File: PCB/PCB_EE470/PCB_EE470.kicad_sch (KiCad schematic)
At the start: 21 parts, among them IC1 LME49860MAX_NOPB, J1 Power, J2 Digital/PWM, J3 Analog, J4 Digital/PWM

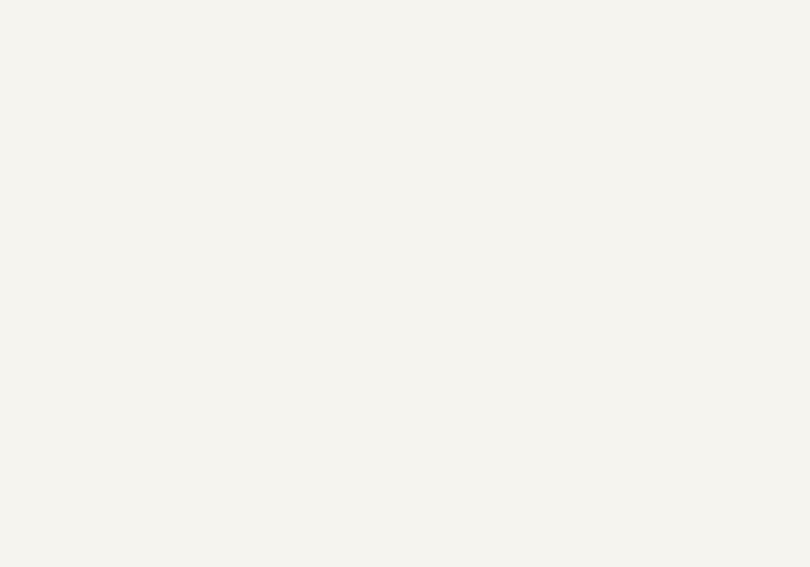
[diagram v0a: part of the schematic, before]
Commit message: ajout port jst écran arduino
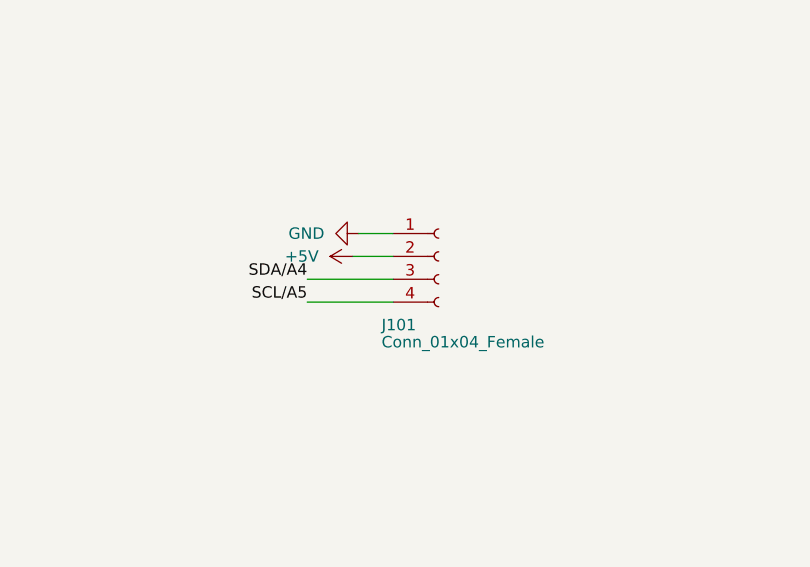
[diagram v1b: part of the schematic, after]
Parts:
- added J101: Conn_01x04_Female, Connector_JST:JST_XH_B4B-XH-A_1x04_P2.50mm_Vertical, symbol Connector:Conn_01x04_Female
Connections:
- net +5V: now also J101.2 (Pin_2)
- net GND: now also J101.1 (Pin_1)
- net SCL/A5: now also J101.4 (Pin_4)
- net SDA/A4: now also J101.3 (Pin_3)
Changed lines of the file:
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@@
+    (stroke (width 0) (type default))
+  )
+  (wire (pts (xy 129.54 71.12) (xy 139.065 71.12))
     (stroke (width 0) (type default))
   )
@@
     (stroke (width 0) (type solid))
   )
+  (wire (pts (xy 134.62 68.58) (xy 139.065 68.58))
+    (stroke (width 0) (type default))
+  )
   (wire (pts (xy 162.56 120.65) (xy 162.56 116.84))
     (stroke (width 0) (type default))
@@
     (stroke (width 0) (type solid))
   )
+  (wire (pts (xy 135.255 66.04) (xy 139.065 66.04))
+    (stroke (width 0) (type default))
+  )
   (wire (pts (xy 152.4 127) (xy 168.91 127))
     (stroke (width 0) (type default))
@@
     (stroke (width 0) (type solid))
   )
+  (wire (pts (xy 129.54 73.66) (xy 139.065 73.66))
+    (stroke (width 0) (type default))
+  )
   (wire (pts (xy 276.86 116.84) (xy 276.86 118.11))
     (stroke (width 0) (type default))
@@
     (effects (font (size 1.27 1.27)) (justify right bottom))
   )
+  (label "SCL{slash}A5" (at 129.54 73.66 180) (fields_autoplaced)
+    (effects (font (size 1.27 1.27)) (justify right bottom))
+  )
   (label "7" (at 279.4 52.07 180) (fields_autoplaced)
     (effects (font (size 1.27 1.27)) (justify right bottom))
@@
   (label "IOREF" (at 223.52 26.67 0) (fields_autoplaced)
     (effects (font (size 1.27 1.27)) (justify left bottom))
+  )
+  (label "SDA{slash}A4" (at 129.54 71.12 180) (fields_autoplaced)
+    (effects (font (size 1.27 1.27)) (justify right bottom))
   )
   (label "SDA{slash}A4" (at 226.06 62.23 0) (fields_autoplaced)
@@
     )
   )
+  (symbol (lib_id "Connector:Conn_01x04_Female") (at 144.145 68.58 0) (unit 1)
+    (in_bom yes) (on_board yes) (dnp no)
+    (property "Reference" "J101" (at 137.795 76.2 0)
+      (effects (font (size 1.27 1.27)) (justify left))
+    )
+    (property "Value" "Conn_01x04_Female" (at 137.795 78.105 0)
+      (effects (font (size 1.27 1.27)) (justify left))
+    )
+    (property "Footprint" "Connector_JST:JST_XH_B4B-XH-A_1x04_P2.50mm_Vertical" (at 144.145 68.58 0)
+      (effects (font (size 1.27 1.27)) hide)
+    )
+    (property "Datasheet" "~" (at 144.145 68.58 0)
+      (effects (font (size 1.27 1.27)) hide)
+    )
+    (pin "3")
+    (pin "2")
+    (pin "1")
+    (pin "4")
+    (instances
+      (project "PCB_EE470"
+        (path "/e63e39d7-6ac0-4ffd-8aa3-1841a4541b55"
+          (reference "J101") (unit 1)
+        )
+      )
+    )
+  )
   (symbol (lib_id "Device:Microphone_Ultrasound") (at 82.55 133.35 0) (unit 1)
     (in_bom yes) (on_board yes) (dnp no)
@@
     )
   )
+  (symbol (lib_id "power:GND") (at 135.255 66.04 270) (unit 1)
+    (in_bom yes) (on_board yes) (dnp no) (fields_autoplaced)
+    (property "Reference" "#PWR0101" (at 128.905 66.04 0)
+      (effects (font (size 1.27 1.27)) hide)
+    )
+    (property "Value" "GND" (at 131.445 66.04 90)
+      (effects (font (size 1.27 1.27)) (justify right))
+    )
+    (property "Footprint" "" (at 135.255 66.04 0)
+      (effects (font (size 1.27 1.27)) hide)
+    )
+    (property "Datasheet" "" (at 135.255 66.04 0)
+      (effects (font (size 1.27 1.27)) hide)
+    )
+    (pin "1")
+    (instances
+      (project "PCB_EE470"
+        (path "/e63e39d7-6ac0-4ffd-8aa3-1841a4541b55"
+          (reference "#PWR0101") (unit 1)
+        )
+      )
+    )
+  )
   (symbol (lib_name "GND_3") (lib_id "power:GND") (at 135.89 139.7 0) (unit 1)
     (in_bom yes) (on_board yes) (dnp no) (fields_autoplaced)
@@
         )
       )
+    )
+  )
+  (symbol (lib_id "power:+5V") (at 134.62 68.58 90) (unit 1)
+    (in_bom yes) (on_board yes) (dnp no) (fields_autoplaced)
+    (property "Reference" "#PWR0102" (at 138.43 68.58 0)
+      (effects (font (size 1.27 1.27)) hide)
+    )
+    (property "Value" "+5V" (at 130.81 68.58 90)
+      (effects (font (size 1.27 1.27)) (justify left))
+    )
+    (property "Footprint" "" (at 134.62 68.58 0)
+      (effects (font (size 1.27 1.27)) hide)
+    )
+    (property "Datasheet" "" (at 134.62 68.58 0)
+      (effects (font (size 1.27 1.27)) hide)
+    )
+    (pin "1")
+    (instances
+      (project "PCB_EE470"
+        (path "/e63e39d7-6ac0-4ffd-8aa3-1841a4541b55"
+          (reference "#PWR0102") (unit 1)
+        )
+      )
